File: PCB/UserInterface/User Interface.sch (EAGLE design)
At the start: 20 parts

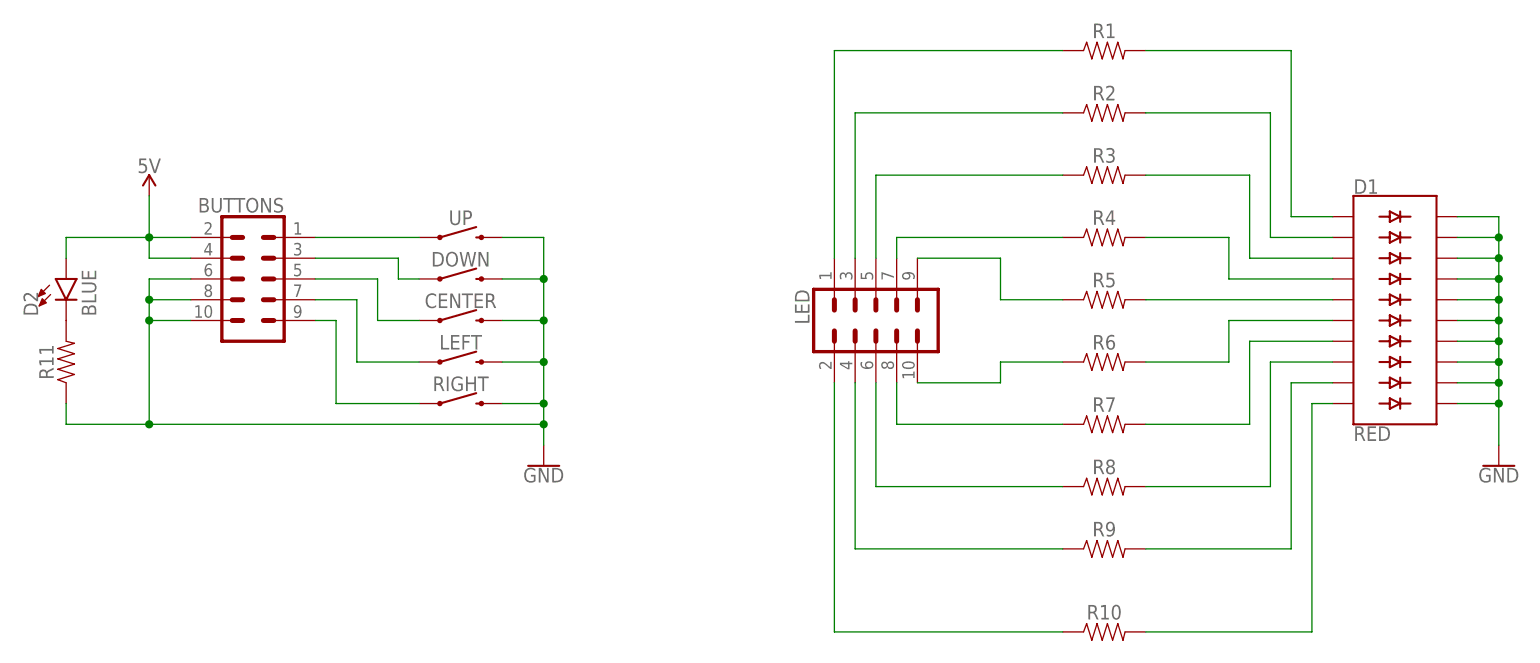
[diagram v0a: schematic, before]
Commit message: update user interface
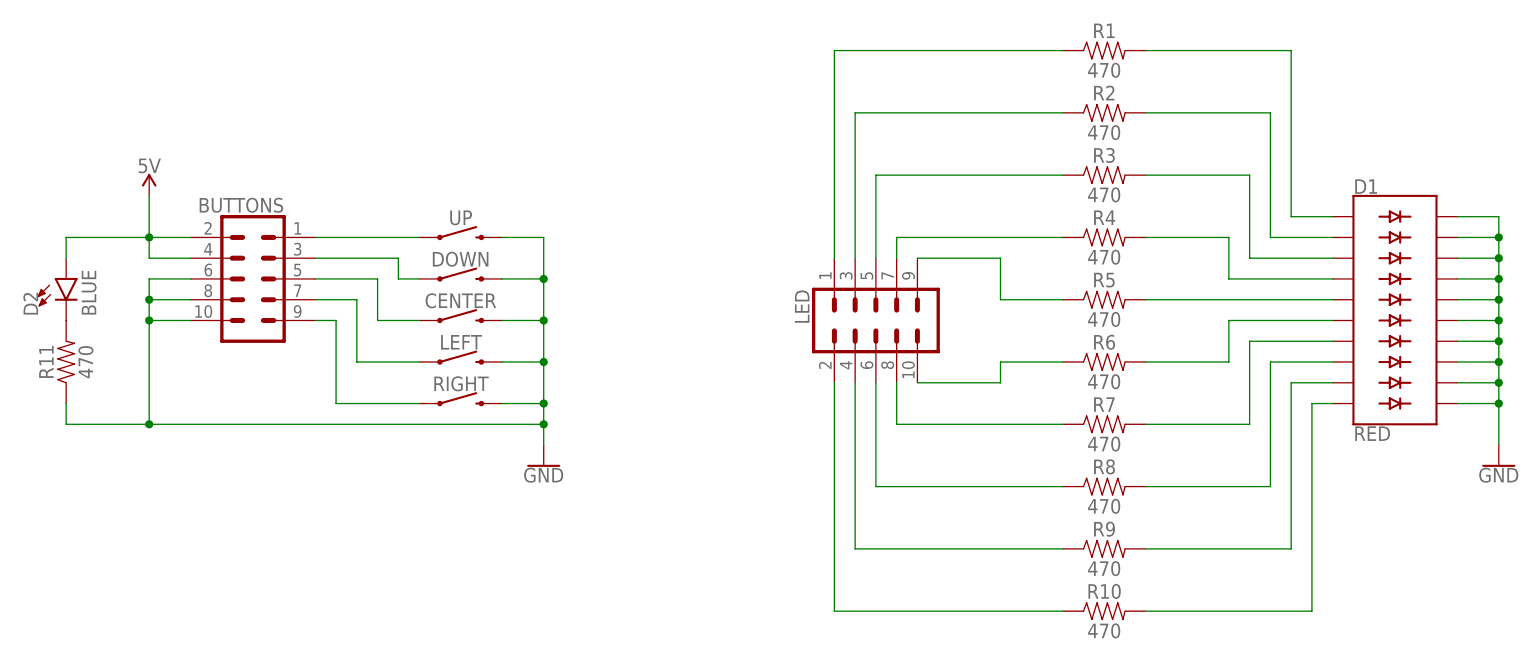
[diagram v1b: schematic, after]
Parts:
- R1, R10, R11, R2, R3, R4, R5, R6, R7, R8, R9: value (none) -> 470
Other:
- moved on the sheet: R10
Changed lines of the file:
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@@
 <part name="BUTTONS" library="SparkFun-Connectors" deviceset="CONN_05X2" device="SHD"/>
 <part name="D1" library="SparkFun-LED" deviceset="LED_BARGRAPH_10" device="RED" value="RED"/>
-<part name="R1" library="SparkFun-Resistors" deviceset="RESISTOR" device="1206" value=" "/>
-<part name="R2" library="SparkFun-Resistors" deviceset="RESISTOR" device="1206" value=" "/>
-<part name="R3" library="SparkFun-Resistors" deviceset="RESISTOR" device="1206" value=" "/>
-<part name="R4" library="SparkFun-Resistors" deviceset="RESISTOR" device="1206" value=" "/>
-<part name="R5" library="SparkFun-Resistors" deviceset="RESISTOR" device="1206" value=" "/>
-<part name="R6" library="SparkFun-Resistors" deviceset="RESISTOR" device="1206" value=" "/>
-<part name="R7" library="SparkFun-Resistors" deviceset="RESISTOR" device="1206" value=" "/>
-<part name="R8" library="SparkFun-Resistors" deviceset="RESISTOR" device="1206" value=" "/>
-<part name="R9" library="SparkFun-Resistors" deviceset="RESISTOR" device="1206" value=" "/>
-<part name="R10" library="SparkFun-Resistors" deviceset="RESISTOR" device="1206" value=" "/>
+<part name="R1" library="SparkFun-Resistors" deviceset="RESISTOR" device="1206" value="470"/>
+<part name="R2" library="SparkFun-Resistors" deviceset="RESISTOR" device="1206" value="470"/>
+<part name="R3" library="SparkFun-Resistors" deviceset="RESISTOR" device="1206" value="470"/>
+<part name="R4" library="SparkFun-Resistors" deviceset="RESISTOR" device="1206" value="470"/>
+<part name="R5" library="SparkFun-Resistors" deviceset="RESISTOR" device="1206" value="470"/>
+<part name="R6" library="SparkFun-Resistors" deviceset="RESISTOR" device="1206" value="470"/>
+<part name="R7" library="SparkFun-Resistors" deviceset="RESISTOR" device="1206" value="470"/>
+<part name="R8" library="SparkFun-Resistors" deviceset="RESISTOR" device="1206" value="470"/>
+<part name="R9" library="SparkFun-Resistors" deviceset="RESISTOR" device="1206" value="470"/>
+<part name="R10" library="SparkFun-Resistors" deviceset="RESISTOR" device="1206" value="470"/>
 <part name="UP" library="SparkFun-Switches" deviceset="MOMENTARY-SWITCH-SPST" device="-PTH-6.0MM"/>
 <part name="DOWN" library="SparkFun-Switches" deviceset="MOMENTARY-SWITCH-SPST" device="-PTH-6.0MM"/>
@@
 <part name="SUPPLY1" library="SparkFun-PowerSymbols" deviceset="5V" device=""/>
 <part name="D2" library="SparkFun-LED" deviceset="LED-BLUE" device="1206" value="BLUE"/>
-<part name="R11" library="SparkFun-Resistors" deviceset="RESISTOR" device="1206" value=" "/>
+<part name="R11" library="SparkFun-Resistors" deviceset="RESISTOR" device="1206" value="470"/>
 </parts>
 <sheets>
@@
 <instance part="R8" gate="G$1" x="177.8" y="86.36"/>
 <instance part="R9" gate="G$1" x="177.8" y="78.74"/>
-<instance part="R10" gate="G$1" x="177.8" y="68.58"/>
+<instance part="R10" gate="G$1" x="177.8" y="71.12"/>
 <instance part="UP" gate="G$1" x="99.06" y="116.84" smashed="yes">
 <attribute name="NAME" x="99.06" y="118.364" size="1.778" layer="95" font="vector" align="bottom-center"/>
@@
 <segment>
 <pinref part="R10" gate="G$1" pin="2"/>
-<wire x1="182.88" y1="68.58" x2="203.2" y2="68.58" width="0.1524" layer="91"/>
-<wire x1="203.2" y1="68.58" x2="203.2" y2="96.52" width="0.1524" layer="91"/>
+<wire x1="182.88" y1="71.12" x2="203.2" y2="71.12" width="0.1524" layer="91"/>
+<wire x1="203.2" y1="71.12" x2="203.2" y2="96.52" width="0.1524" layer="91"/>
 <pinref part="D1" gate="G$1" pin="A9"/>
 <wire x1="203.2" y1="96.52" x2="205.74" y2="96.52" width="0.1524" layer="91"/>
@@
 <segment>
 <pinref part="LED" gate="G$1" pin="2"/>
-<wire x1="144.78" y1="99.06" x2="144.78" y2="68.58" width="0.1524" layer="91"/>
+<wire x1="144.78" y1="99.06" x2="144.78" y2="71.12" width="0.1524" layer="91"/>
 <pinref part="R10" gate="G$1" pin="1"/>
-<wire x1="144.78" y1="68.58" x2="172.72" y2="68.58" width="0.1524" layer="91"/>
-</segment>
-</net>
+<wire x1="144.78" y1="71.12" x2="172.72" y2="71.12" width="0.1524" layer="91"/>
+</segment>
+</net>
